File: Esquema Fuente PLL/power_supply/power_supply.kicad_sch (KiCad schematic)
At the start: 0 parts

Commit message: se agrega nuevo proyecto
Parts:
- added C1: 0.1uF, Capacitor_THT:CP_Radial_D10.0mm_P5.00mm, symbol Device:C_Polarized
- added C2: 0.1uF, symbol Device:C_Polarized
- added D1, D2: 1N4007, Diode_THT:D_DO-41_SOD81_P10.16mm_Horizontal, symbol Diode:1N4007
- added D3: 1N4733A, Diode_THT:D_DO-41_SOD81_P10.16mm_Horizontal, symbol Diode:1N47xxA
- added D4, D6: Q_SCR_AGK, symbol Device:Q_SCR_AGK
- added D5: BZV55C12, Diode_SMD:D_MiniMELF, symbol Diode:BZV55C12
- added F1, F2: Fuse, symbol Device:Fuse
- added J1: Screw_Terminal_01x02, TerminalBlock_MetzConnect:TerminalBlock_MetzConnect_Type011_RT05502HBLC_1x02_P5.00mm_Horizontal, symbol Connector:Screw_Terminal_01x02
- added J2, J3: Screw_Terminal_01x02, symbol Connector:Screw_Terminal_01x02
- added PS1: HLK-10M12, Converter_ACDC:Converter_ACDC_Hi-Link_HLK-10Mxx, symbol Converter_ACDC:HLK-10M12
- added PS2: HLK-PM01, Converter_ACDC:Converter_ACDC_Hi-Link_HLK-PMxx, symbol Converter_ACDC:HLK-PM01
- added R1: 1k, Resistor_THT:R_Axial_DIN0207_L6.3mm_D2.5mm_P10.16mm_Horizontal, symbol Device:R
- added R2: 1k, symbol Device:R
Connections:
- new net: D3.1 (K), D4.1 (A), F2.2, J3.2 (Pin_2)
- new net: C1.1, D3.2 (A), D4.2 (G), R1.1
- new net: C2.1, D5.2 (A), D6.2 (G), R2.1
- new net: J1.1 (Pin_1), PS1.1 (AC/L), PS2.1 (AC/L)
- new net: J1.2 (Pin_2), PS1.2 (AC/N), PS2.2 (AC/N)
- new net: D5.1 (K), D6.1 (A), F1.2, J2.2 (Pin_2)
- new net +12V: D1.1 (K), F1.1, PS1.4 (+Vout)
- new net +5V: D2.1 (K), F2.1, PS2.4 (+Vout)
- new net GND: C1.2, C2.2, D1.2 (A), D2.2 (A), D4.3 (K), D6.3 (K), J2.1 (Pin_1), J3.1 (Pin_1), PS1.3 (-Vout), PS2.3 (-Vout), R1.2, R2.2

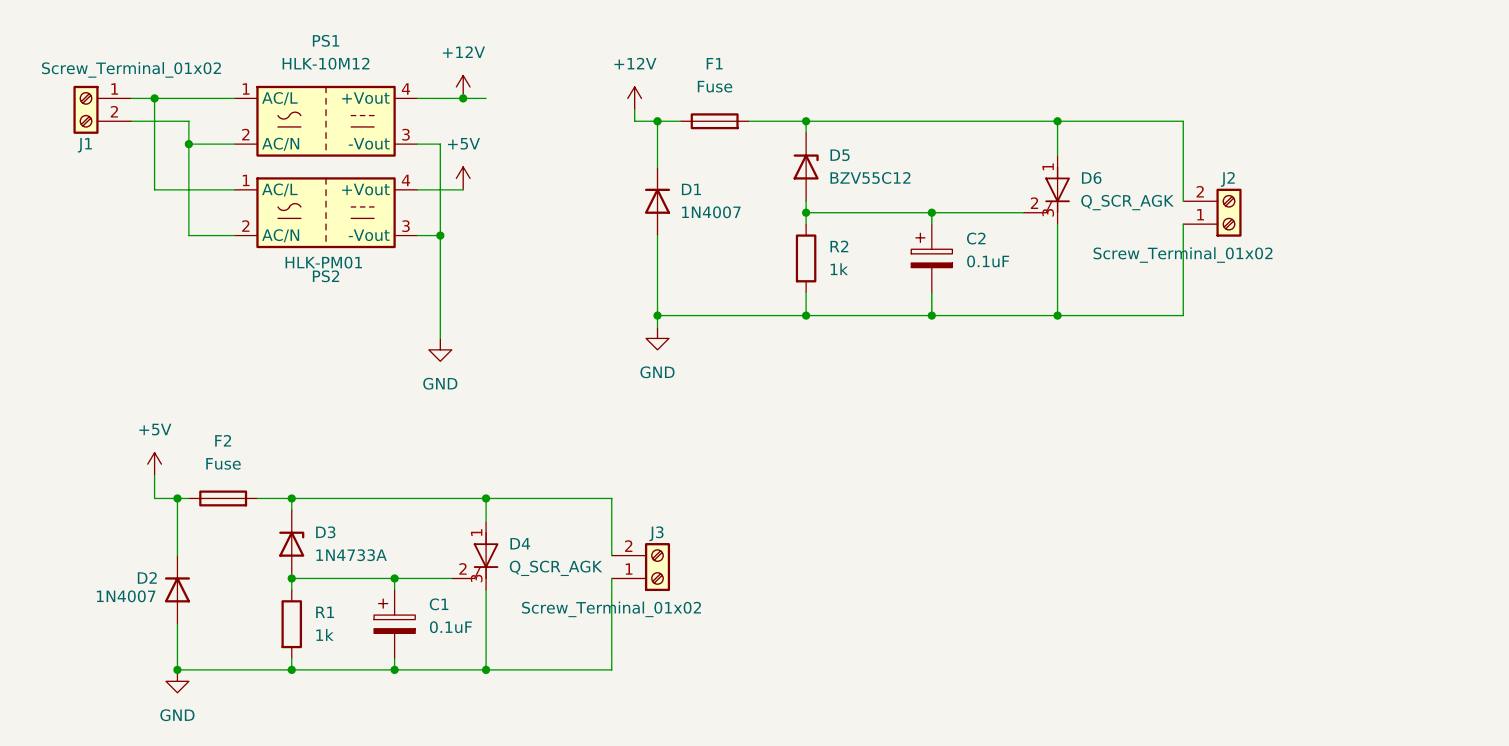
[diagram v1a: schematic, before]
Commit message: Se agrega los links hacia los datasheet para los distintos elementos usados, se actualiza el esquemático
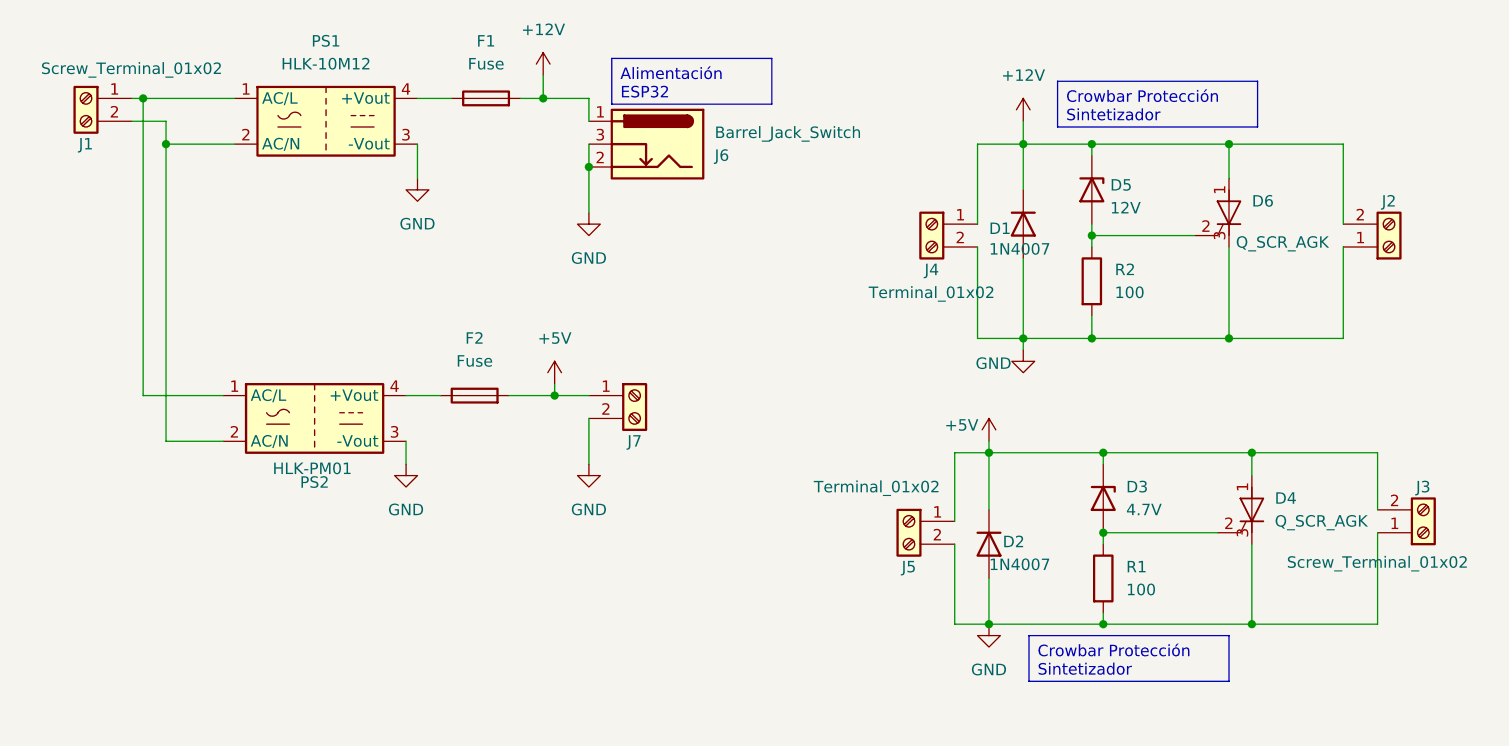
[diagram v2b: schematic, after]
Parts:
- removed C1: 0.1uF, Capacitor_THT:CP_Radial_D10.0mm_P5.00mm, symbol Device:C_Polarized
- removed C2: 0.1uF, symbol Device:C_Polarized
- added J4, J5, J7: Terminal_01x02, symbol Connector:Screw_Terminal_01x02
- added J6: Barrel_Jack_Switch, Connector_BarrelJack:BarrelJack_GCT_DCJ200-10-A_Horizontal, symbol Connector:Barrel_Jack_Switch
- D3: value 1N4733A -> 4.7V
- D5: value BZV55C12 -> 12V
- J2: value Screw_Terminal_01x02 -> Terminal_01x02
- R1: value 1k -> 100
- R2: value 1k -> 100; footprint (none) -> Resistor_THT:R_Axial_DIN0207_L6.3mm_D2.5mm_P10.16mm_Horizontal
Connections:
- net +12V: now also D5.1 (K), D6.1 (A), F1.2, J2.2 (Pin_2), J4.1 (Pin_1), J6.1; no longer F1.1, PS1.4 (+Vout)
- net +5V: now also D3.1 (K), D4.1 (A), F2.2, J3.2 (Pin_2), J5.1 (Pin_1), J7.1 (Pin_1); no longer F2.1, PS2.4 (+Vout)
- net GND: now also J4.2 (Pin_2), J5.2 (Pin_2), J6.2, J6.3, J7.2 (Pin_2)
- new net: F2.1, PS2.4 (+Vout)
- new net: F1.1, PS1.4 (+Vout)
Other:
- moved on the sheet: D1, D2, D3, D4, D5, D6, F1, F2, J2, J3, PS2, R1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

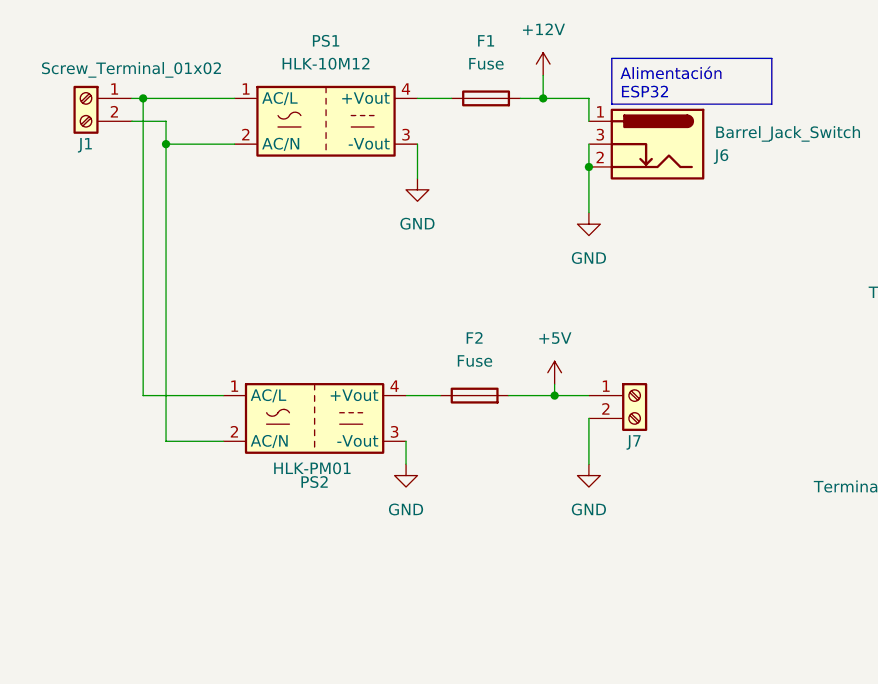
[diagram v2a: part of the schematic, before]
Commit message: Se agrega solo el Esquema Fuente para el sintetizador
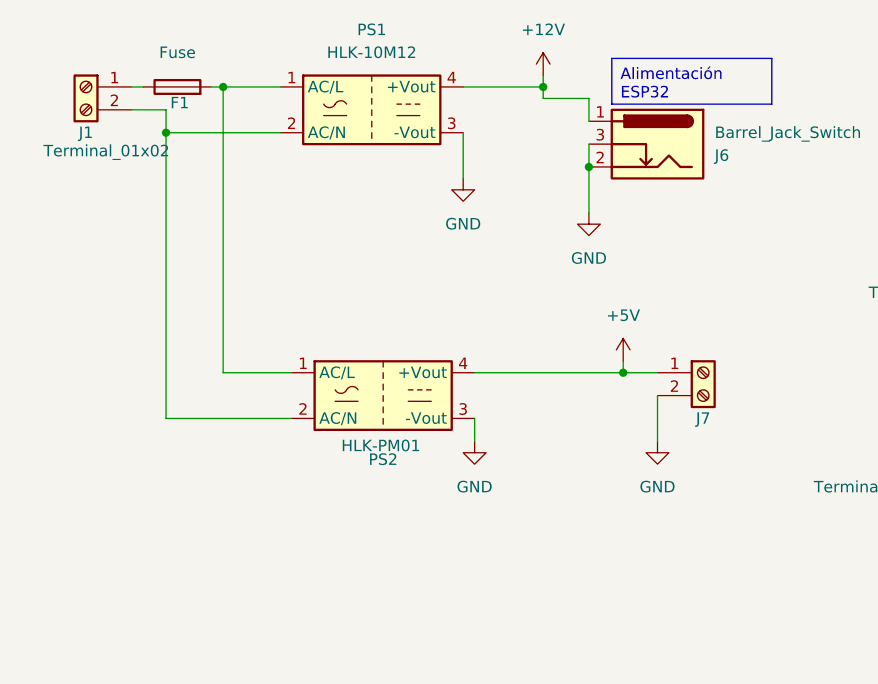
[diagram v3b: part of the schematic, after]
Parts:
- removed F2: Fuse, symbol Device:Fuse
- F1: footprint (none) -> Fuse:Fuseholder_Cylinder-5x20mm_Schurter_0031_8201_Horizontal_Open
- J1: value Screw_Terminal_01x02 -> Terminal_01x02
- J7: footprint (none) -> TerminalBlock_MetzConnect:TerminalBlock_MetzConnect_Type011_RT05502HBLC_1x02_P5.00mm_Horizontal
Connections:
- net +12V: now also PS1.4 (+Vout); no longer F1.2
- net +5V: now also PS2.4 (+Vout)
- net at PS1.1 (AC/L), PS2.1 (AC/L): now also F1.2; no longer J1.1 (Pin_1)
- net at F1.1: now also J1.1 (Pin_1); no longer PS1.4 (+Vout)
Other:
- moved on the sheet: F1, J1, J7, PS1, PS2

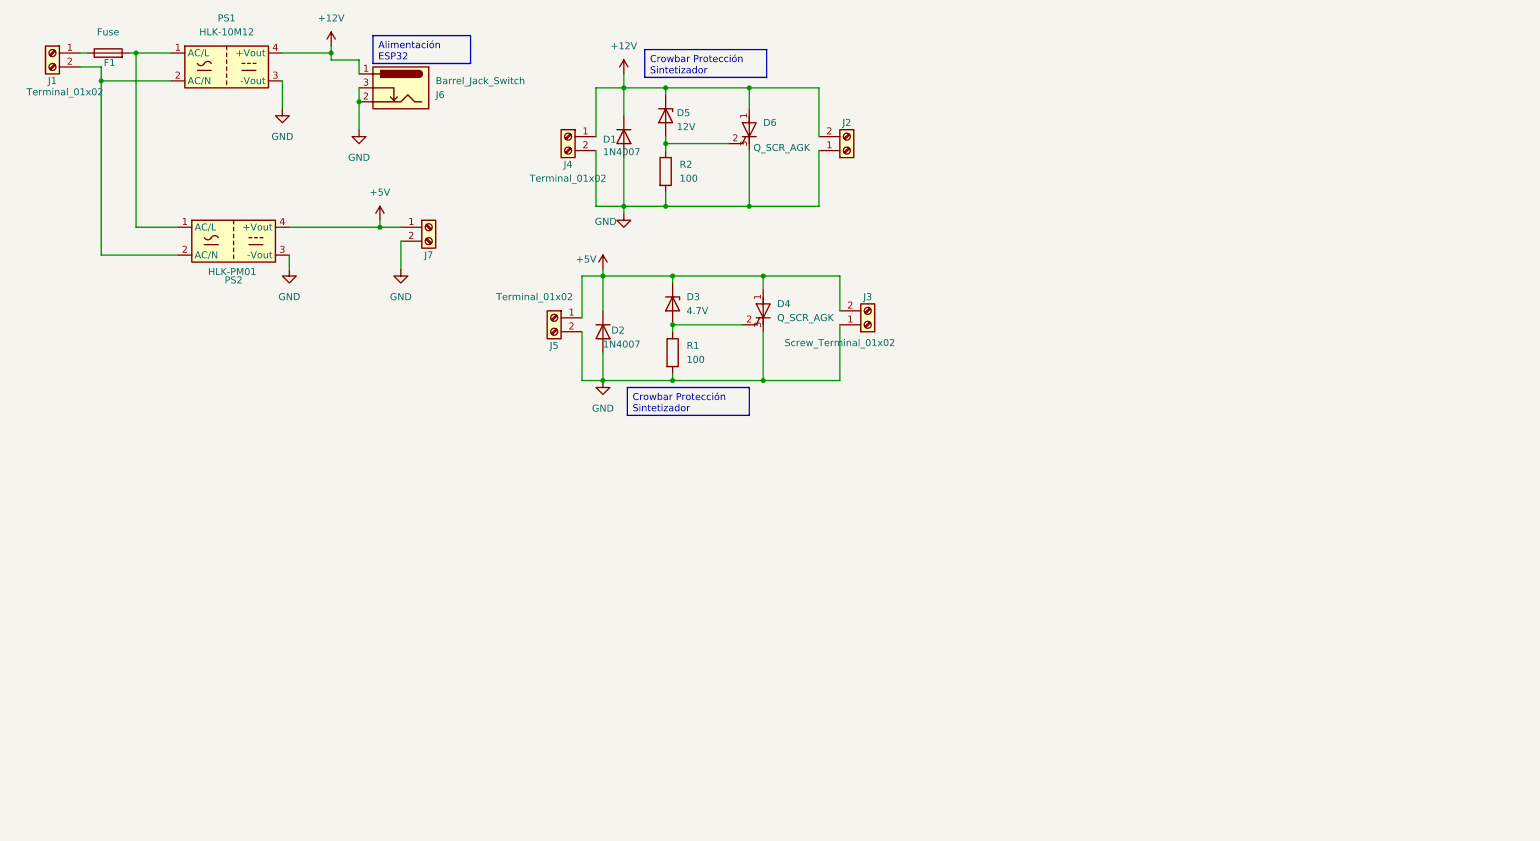
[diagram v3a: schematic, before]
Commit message: se realizaron cambios en el esquema, se agrega un varistor y se hace una div entre parte fria y caliente
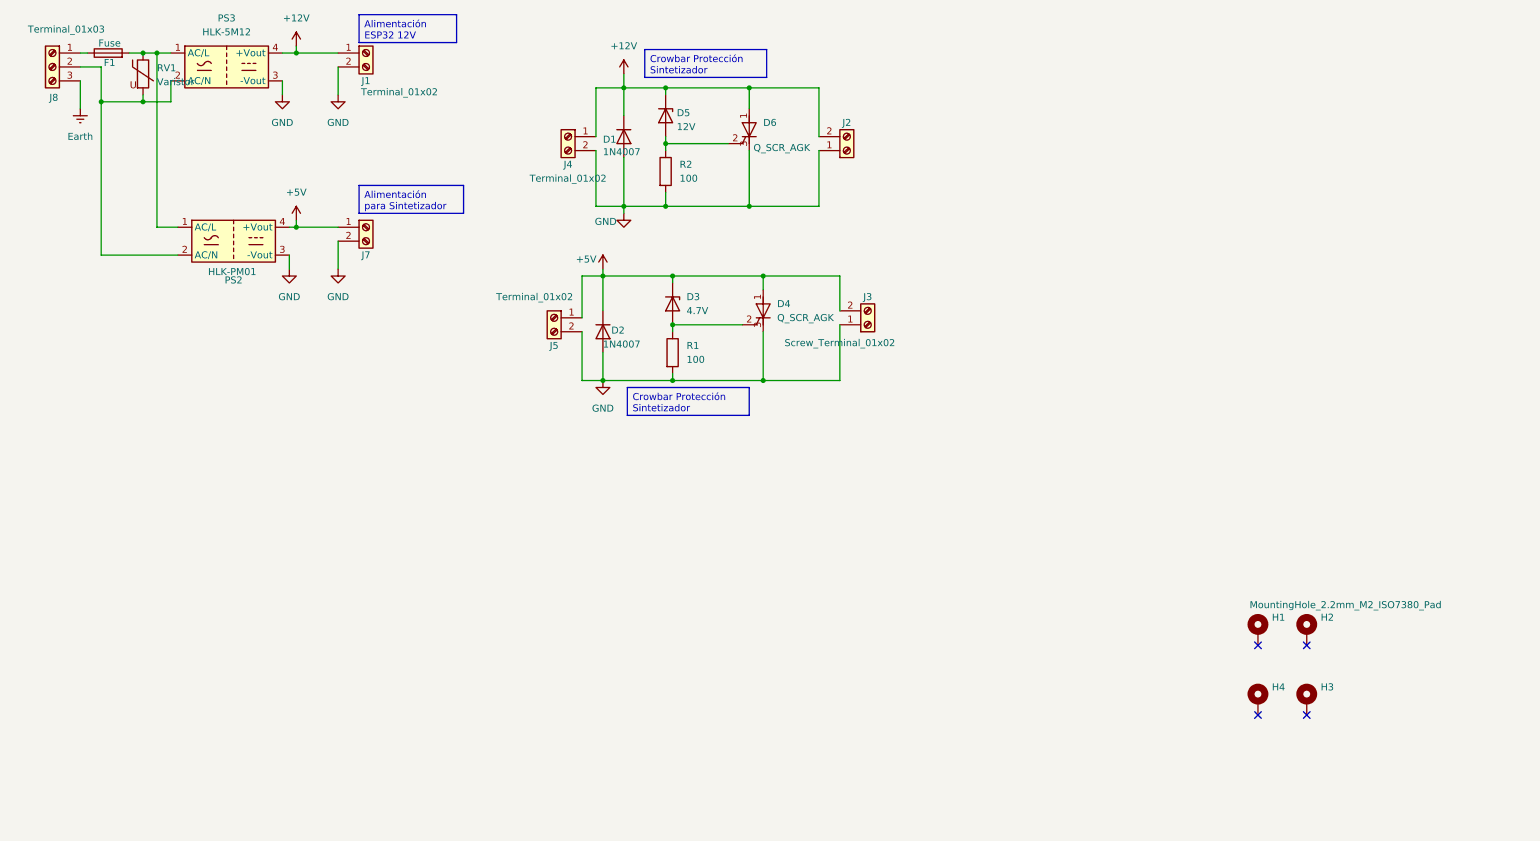
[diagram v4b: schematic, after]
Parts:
- removed J6: Barrel_Jack_Switch, Connector_BarrelJack:BarrelJack_GCT_DCJ200-10-A_Horizontal, symbol Connector:Barrel_Jack_Switch
- removed PS1: HLK-10M12, Converter_ACDC:Converter_ACDC_Hi-Link_HLK-10Mxx, symbol Converter_ACDC:HLK-10M12
- added H1, H2, H3, H4: MountingHole_2.2mm_M2_ISO7380_Pad, MountingHole:MountingHole_2.2mm_M2_ISO7380_Pad, symbol Mechanical:MountingHole_Pad
- added J8: Terminal_01x03, TerminalBlock:TerminalBlock_MaiXu_MX126-5.0-03P_1x03_P5.00mm, symbol Connector:Screw_Terminal_01x03
- added PS3: HLK-5M12, Converter_ACDC:Converter_ACDC_Hi-Link_HLK-5Mxx, symbol Converter_ACDC:HLK-5M12
- added RV1: Varistor, Varistor:RV_Disc_D12mm_W4.2mm_P7.5mm, symbol Device:Varistor
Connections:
- net +12V: now also J1.1 (Pin_1), PS3.4 (+Vout)
- net GND: now also J1.2 (Pin_2), PS3.3 (-Vout)
- net at F1.2, PS2.1 (AC/L): now also PS3.1 (AC/L), RV1.1
- net at PS2.2 (AC/N): now also J8.2 (Pin_2), PS3.2 (AC/N), RV1.2; no longer J1.2 (Pin_2)
- net at F1.1: now also J8.1 (Pin_1); no longer J1.1 (Pin_1)
- new net Earth: J8.3 (Pin_3)
- no-connect marks 0 -> 4
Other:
- moved on the sheet: J1, J7

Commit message: Se agrega pcb de crowbar
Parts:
- removed D4, D6: Q_SCR_AGK, symbol Device:Q_SCR_AGK
- removed J2, J4, J5: Terminal_01x02, symbol Connector:Screw_Terminal_01x02
- removed J3: Screw_Terminal_01x02, symbol Connector:Screw_Terminal_01x02
- added D7: Q_SCR_KGA, Package_TO_SOT_THT:TO-92_Wide, symbol Device:Q_SCR_KGA
- added D8: Q_SCR_KGA, Package_TO_SOT_THT:TO-92L_Wide, symbol Device:Q_SCR_KGA
- added H5, H6, H7, H8: MountingHole_2.2mm_M2_ISO7380_Pad, MountingHole:MountingHole_2.2mm_M2_ISO7380_Pad, symbol Mechanical:MountingHole_Pad
- added J2: 01x03, TerminalBlock:TerminalBlock_MaiXu_MX126-5.0-03P_1x03_P5.00mm, symbol Connector:Screw_Terminal_01x03
- D5: footprint Diode_SMD:D_MiniMELF -> Diode_THT:D_DO-41_SOD81_P10.16mm_Horizontal
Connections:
- net +12V: now also D8.3 (A), J2.1 (Pin_1)
- net +5V: now also D7.3 (A), J2.3 (Pin_3)
- net GND: now also D7.1 (K), D8.1 (K), J2.2 (Pin_2)
- net at D3.2 (A), R1.1: now also D7.2 (G)
- net at D5.2 (A), R2.1: now also D8.2 (G)
- no-connect marks 4 -> 8
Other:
- moved on the sheet: D2, D3, H1, H2, H3, H4, R1
